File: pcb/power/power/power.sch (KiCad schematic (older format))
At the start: 14 parts, among them J1001 Conn_01x03_Female, J1002 Conn_01x04_Female, J1003 Conn_01x03_Female

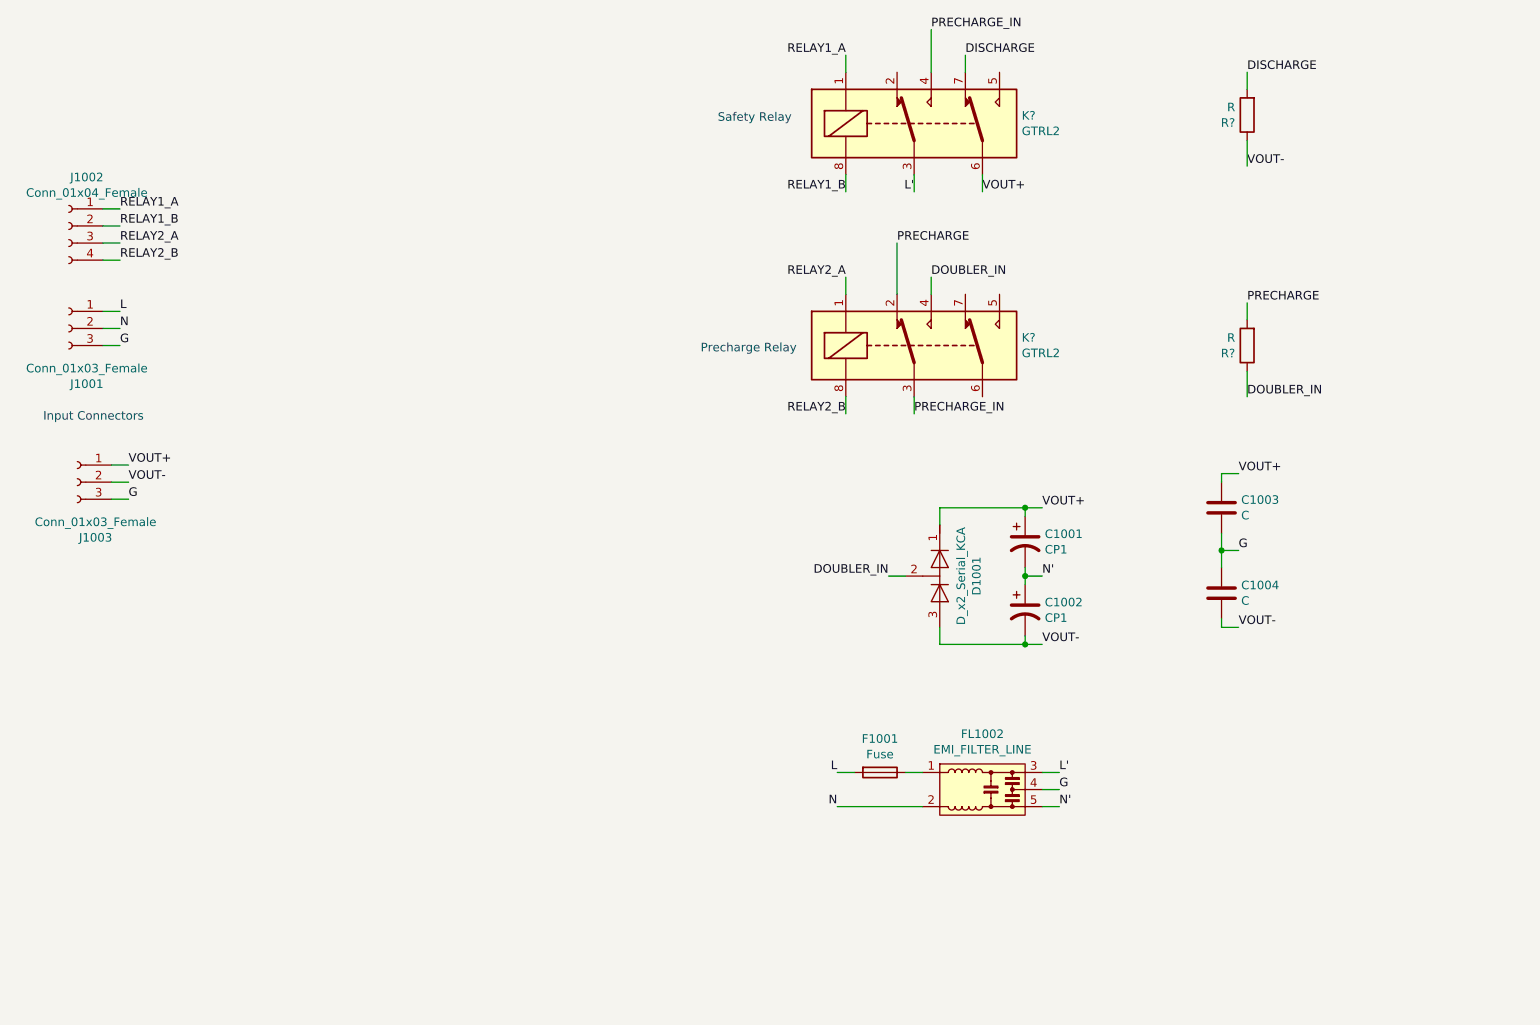
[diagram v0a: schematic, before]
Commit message: finished power and MMC PCBs and created gerbers
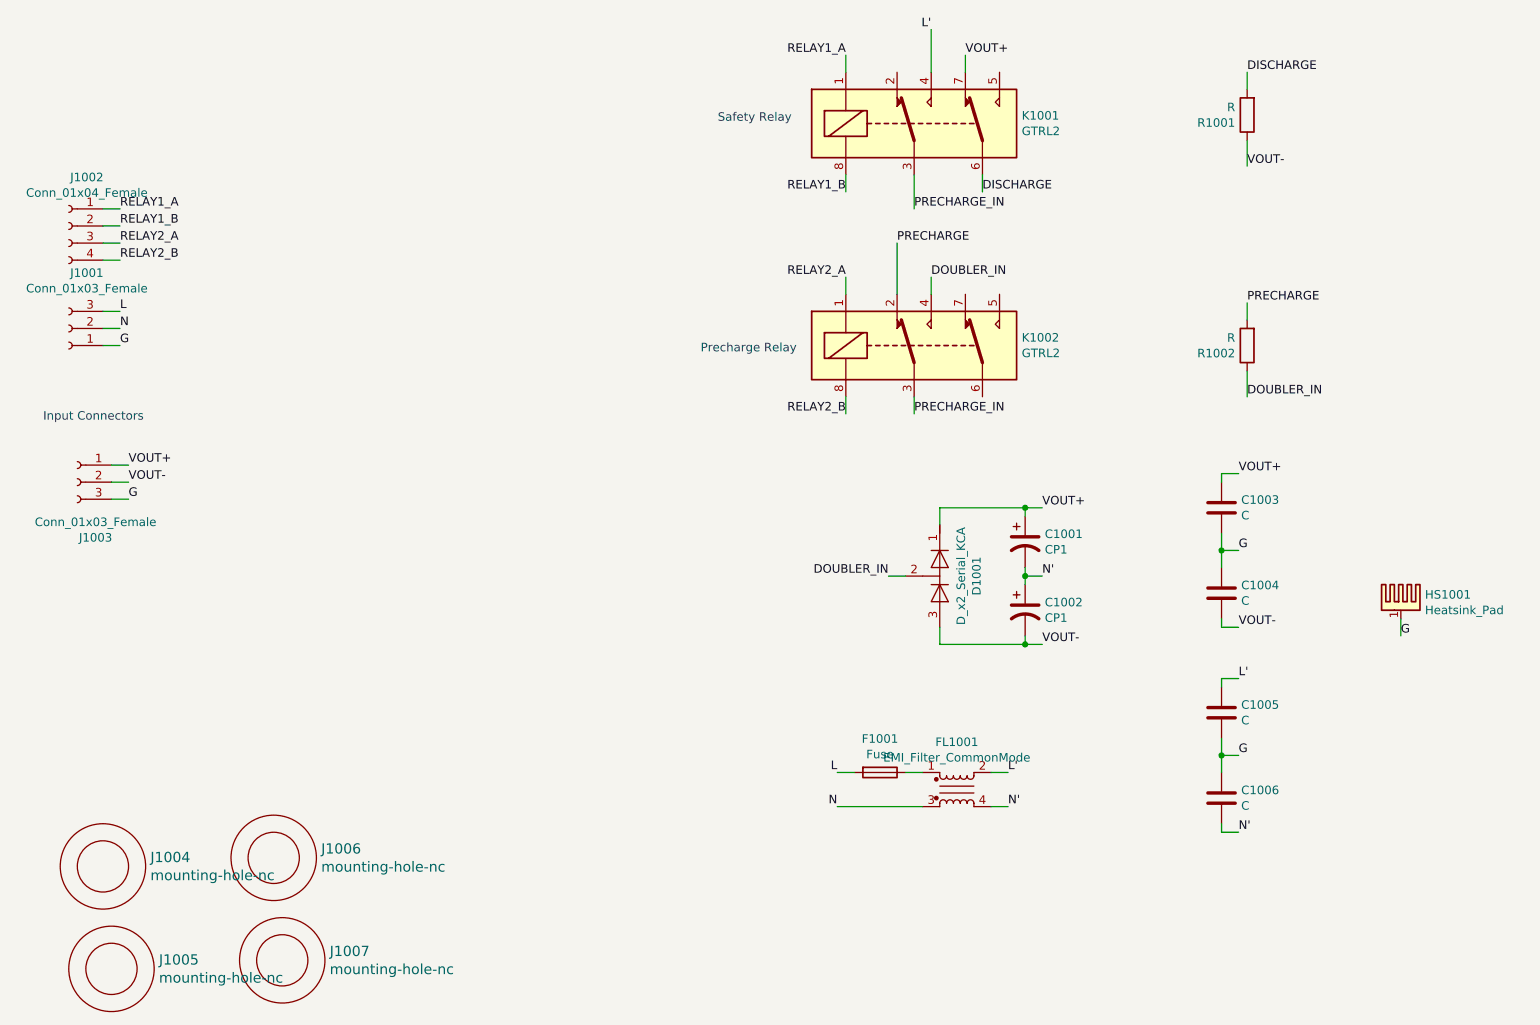
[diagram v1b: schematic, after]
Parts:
- removed FL1002: EMI_FILTER_LINE, symbol wbraun_ic_lib:EMI_FILTER_LINE
- added C1005, C1006: C, Capacitor_THT:C_Rect_L18.0mm_W8.0mm_P15.00mm_FKS3_FKP3, symbol Device:C
- added FL1001: EMI_Filter_CommonMode, wbraun_smd:744824622, symbol Device:EMI_Filter_CommonMode
- added HS1001: Heatsink_Pad, wbraun_smd:RA-T2X, symbol Mechanical:Heatsink_Pad
- added J1004, J1005, J1006, J1007: mounting-hole-nc, wbraun_smd:M3-mounting-hole-insulated, symbol wbraun_ic_lib:mounting-hole-nc
- C1001, C1002: footprint (none) -> Capacitor_THT:CP_Radial_D25.0mm_P10.00mm_SnapIn
- C1003, C1004: footprint (none) -> Capacitor_THT:C_Rect_L18.0mm_W8.0mm_P15.00mm_FKS3_FKP3
- D1001: footprint (none) -> Package_TO_SOT_THT:TO-247-3_Vertical
- J1001, J1003: footprint (none) -> wbraun_smd:Terminal-block-plug_3x1_5mm-pitch
- J1002: footprint (none) -> wbraun_smd:Terminal-block-plug_4x1_3.5mm-pitch
- K1001, K1002: renamed from K?; footprint (none) -> wbraun_smd:G2RL-2
- R1001, R1002: renamed from R?; footprint (none) -> wbraun_smd:RESISTOR_CW010
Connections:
- net DISCHARGE: now also K1001.6; no longer K1001.7
- net G: now also J1001.1 (Pin_1), C1005.2, C1006.1, HS1001.1; no longer J1001.3 (Pin_3)
- net L: now also J1001.3 (Pin_3); no longer J1001.1 (Pin_1)
- net L': now also K1001.4, C1005.1, FL1001.2; no longer K1001.3
- net N: now also FL1001.3
- net N': now also C1006.2, FL1001.4
- net PRECHARGE_IN: now also K1001.3; no longer K1001.4
- net VOUT+: now also K1001.7; no longer K1001.6
- net at F1001.1: now also FL1001.1
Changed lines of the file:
@@
 EESchema Schematic File Version 4
+LIBS:power-cache
 EELAYER 26 0
 EELAYER END
@@
 F 0 "J1002" H 1944 2285 50  0000 C CNN
 F 1 "Conn_01x04_Female" H 1944 2194 50  0000 C CNN
-F 2 "" H 2050 2000 50  0001 C CNN
+F 2 "wbraun_smd:Terminal-block-plug_4x1_3.5mm-pitch" H 2050 2000 50  0001 C CNN
 F 3 "~" H 2050 2000 50  0001 C CNN
 	1    2050 2000
@@
 F 0 "C1001" H 7765 3896 50  0000 L CNN
 F 1 "CP1" H 7765 3805 50  0000 L CNN
-F 2 "" H 7650 3850 50  0001 C CNN
+F 2 "Capacitor_THT:CP_Radial_D25.0mm_P10.00mm_SnapIn" H 7650 3850 50  0001 C CNN
 F 3 "~" H 7650 3850 50  0001 C CNN
 	1    7650 3850
@@
 F 0 "D1001" H 7150 4266 50  0000 C CNN
 F 1 "D_x2_Serial_KCA" H 7150 4175 50  0000 C CNN
-F 2 "" H 7150 4050 50  0001 C CNN
+F 2 "Package_TO_SOT_THT:TO-247-3_Vertical" H 7150 4050 50  0001 C CNN
 F 3 "~" H 7150 4050 50  0001 C CNN
 	1    7150 4050
@@
 F 0 "C1003" H 8915 3696 50  0000 L CNN
 F 1 "C" H 8915 3605 50  0000 L CNN
-F 2 "" H 8838 3500 50  0001 C CNN
+F 2 "Capacitor_THT:C_Rect_L18.0mm_W8.0mm_P15.00mm_FKS3_FKP3" H 8838 3500 50  0001 C CNN
 F 3 "~" H 8800 3650 50  0001 C CNN
 	1    8800 3650
@@
 F 0 "C1004" H 8915 4196 50  0000 L CNN
 F 1 "C" H 8915 4105 50  0000 L CNN
-F 2 "" H 8838 4000 50  0001 C CNN
+F 2 "Capacitor_THT:C_Rect_L18.0mm_W8.0mm_P15.00mm_FKS3_FKP3" H 8838 4000 50  0001 C CNN
 F 3 "~" H 8800 4150 50  0001 C CNN
 	1    8800 4150
@@
 F 0 "J1001" H 1944 2275 50  0000 C CNN
 F 1 "Conn_01x03_Female" H 1944 2366 50  0000 C CNN
-F 2 "" H 2050 2600 50  0001 C CNN
+F 2 "wbraun_smd:Terminal-block-plug_3x1_5mm-pitch" H 2050 2600 50  0001 C CNN
 F 3 "~" H 2050 2600 50  0001 C CNN
 	1    2050 2600
-	-1   0    0    -1
-$EndComp
-$Comp
-L wbraun_ic_lib:EMI_FILTER_LINE FL1002
-U 1 1 5C48EEA0
-P 7400 5300
-F 0 "FL1002" H 7400 5625 50  0000 C CNN
-F 1 "EMI_FILTER_LINE" H 7400 5534 50  0000 C CNN
-F 2 "" H 7400 5300 50  0001 C CNN
-F 3 "" H 7400 5300 50  0001 C CNN
-	1    7400 5300
-	1    0    0    -1
+	-1   0    0    1
 $EndComp
 $Comp
@@
 	6650 5200 6550 5200
 Wire Wire Line
-	7750 5200 7850 5200
-Wire Wire Line
-	7750 5300 7850 5300
-Wire Wire Line
-	7750 5400 7850 5400
+	7450 5200 7550 5200
+Wire Wire Line
+	7450 5400 7550 5400
 Text Label 6550 5200 2    50   ~ 0
 L
 Text Label 6550 5400 2    50   ~ 0
 N
-Text Label 7850 5200 0    50   ~ 0
+Text Label 7550 5200 0    50   ~ 0
 L'
-Text Label 7850 5400 0    50   ~ 0
+Text Label 7550 5400 0    50   ~ 0
 N'
-Text Label 7850 5300 0    50   ~ 0
-G
-$Comp
-L wbraun_ic_lib:GTRL2 K?
+$Comp
+L wbraun_ic_lib:GTRL2 K1001
 U 1 1 5C496070
 P 7000 1400
-F 0 "K?" H 7630 1446 50  0000 L CNN
+F 0 "K1001" H 7630 1446 50  0000 L CNN
 F 1 "GTRL2" H 7630 1355 50  0000 L CNN
-F 2 "" H 6950 1400 50  0001 C CNN
+F 2 "wbraun_smd:G2RL-2" H 6950 1400 50  0001 C CNN
 F 3 "" H 6950 1400 50  0001 C CNN
 	1    7000 1400
@@
 $EndComp
 $Comp
-L wbraun_ic_lib:GTRL2 K?
+L wbraun_ic_lib:GTRL2 K1002
 U 1 1 5C4963A0
 P 7000 2700
-F 0 "K?" H 7630 2746 50  0000 L CNN
+F 0 "K1002" H 7630 2746 50  0000 L CNN
 F 1 "GTRL2" H 7630 2655 50  0000 L CNN
-F 2 "" H 6950 2700 50  0001 C CNN
+F 2 "wbraun_smd:G2RL-2" H 6950 2700 50  0001 C CNN
 F 3 "" H 6950 2700 50  0001 C CNN
 	1    7000 2700
@@
 Text Label 6600 1800 2    50   ~ 0
 RELAY1_B
-Wire Wire Line
-	7000 1700 7000 1800
-Text Label 7000 1800 2    50   ~ 0
+Text Label 7100 850  2    50   ~ 0
 L'
 Wire Wire Line
@@
 Wire Wire Line
 	7300 1100 7300 1000
+Text Label 7300 1000 0    50   ~ 0
+VOUT+
 Text Label 7400 1800 0    50   ~ 0
-VOUT+
-Text Label 7300 1000 0    50   ~ 0
 DISCHARGE
 Text Label 7000 3100 0    50   ~ 0
@@
 Wire Wire Line
 	7100 2400 7100 2300
-Text Label 7100 850  0    50   ~ 0
+Text Label 7000 1900 0    50   ~ 0
 PRECHARGE_IN
 Wire Wire Line
@@
 DOUBLER_IN
 $Comp
-L Device:R R?
+L Device:R R1001
 U 1 1 5C498F2D
 P 8950 1350
-F 0 "R?" H 9020 1396 50  0000 L CNN
+F 0 "R1001" H 9020 1396 50  0000 L CNN
 F 1 "R" H 9020 1305 50  0000 L CNN
-F 2 "" V 8880 1350 50  0001 C CNN
+F 2 "wbraun_smd:RESISTOR_CW010" V 8880 1350 50  0001 C CNN
 F 3 "~" H 8950 1350 50  0001 C CNN
 	1    8950 1350
@@
 VOUT-
 $Comp
-L Device:R R?
+L Device:R R1002
 U 1 1 5C499891
 P 8950 2700
-F 0 "R?" H 9020 2746 50  0000 L CNN
+F 0 "R1002" H 9020 2746 50  0000 L CNN
 F 1 "R" H 9020 2655 50  0000 L CNN
-F 2 "" V 8880 2700 50  0001 C CNN
+F 2 "wbraun_smd:RESISTOR_CW010" V 8880 2700 50  0001 C CNN
 F 3 "~" H 8950 2700 50  0001 C CNN
 	1    8950 2700
@@
 F 0 "C1002" H 7765 4296 50  0000 L CNN
 F 1 "CP1" H 7765 4205 50  0000 L CNN
-F 2 "" H 7650 4250 50  0001 C CNN
+F 2 "Capacitor_THT:CP_Radial_D25.0mm_P10.00mm_SnapIn" H 7650 4250 50  0001 C CNN
 F 3 "~" H 7650 4250 50  0001 C CNN
 	1    7650 4250
@@
 N'
 Wire Wire Line
-	8800 3800 8800 3900
-Wire Wire Line
 	8800 3900 8900 3900
-Connection ~ 8800 3900
-Wire Wire Line
-	8800 3900 8800 4000
 Wire Wire Line
 	8800 3500 8800 3450
@@
 F 0 "J1003" H 1993 3175 50  0000 C CNN
 F 1 "Conn_01x03_Female" H 1993 3266 50  0000 C CNN
-F 2 "" H 2100 3500 50  0001 C CNN
+F 2 "wbraun_smd:Terminal-block-plug_3x1_5mm-pitch" H 2100 3500 50  0001 C CNN
 F 3 "~" H 2100 3500 50  0001 C CNN
 	1    2100 3500
@@
 Text Label 2400 3600 0    50   ~ 0
 G
+$Comp
+L Mechanical:Heatsink_Pad HS1001
+U 1 1 5C4B8180
+P 9850 4200
+F 0 "HS1001" H 9991 4241 50  0000 L CNN
+F 1 "Heatsink_Pad" H 9991 4150 50  0000 L CNN
+F 2 "wbraun_smd:RA-T2X" H 9862 4150 50  0001 C CNN
+F 3 "~" H 9862 4150 50  0001 C CNN
+	1    9850 4200
+	1    0    0    -1
+$EndComp
+$Comp
+L Device:EMI_Filter_CommonMode FL1001
+U 1 1 5C4AA415
+P 7250 5300
+F 0 "FL1001" H 7250 5578 50  0000 C CNN
+F 1 "EMI_Filter_CommonMode" H 7250 5487 50  0000 C CNN
+F 2 "wbraun_smd:744824622" V 7250 5340 50  0001 C CNN
+F 3 "~" V 7250 5340 50  0000 C CNN
+	1    7250 5300
+	1    0    0    -1
+$EndComp
+Wire Wire Line
+	8800 3800 8800 3900
+Wire Wire Line
+	8800 3900 8800 4000
+Connection ~ 8800 3900
+Text Label 9850 4400 0    50   ~ 0
+G
+Wire Wire Line
+	9850 4300 9850 4400
+$Comp
+L wbraun_ic_lib:mounting-hole-nc J1004
+U 1 1 5C4AE651
+P 2250 5750
+F 0 "J1004" H 2528 5803 60  0000 L CNN
+F 1 "mounting-hole-nc" H 2528 5697 60  0000 L CNN
+F 2 "wbraun_smd:M3-mounting-hole-insulated" H 2250 5750 60  0001 C CNN
+F 3 "" H 2250 5750 60  0001 C CNN
+	1    2250 5750
+	1    0    0    -1
+$EndComp
+$Comp
+L wbraun_ic_lib:mounting-hole-nc J1006
+U 1 1 5C4AE7C3
+P 3250 5700
+F 0 "J1006" H 3528 5753 60  0000 L CNN
+F 1 "mounting-hole-nc" H 3528 5647 60  0000 L CNN
+F 2 "wbraun_smd:M3-mounting-hole-insulated" H 3250 5700 60  0001 C CNN
+F 3 "" H 3250 5700 60  0001 C CNN
+	1    3250 5700
+	1    0    0    -1
+$EndComp
+$Comp
+L wbraun_ic_lib:mounting-hole-nc J1007
+U 1 1 5C4AE82D
+P 3300 6300
+F 0 "J1007" H 3578 6353 60  0000 L CNN
+F 1 "mounting-hole-nc" H 3578 6247 60  0000 L CNN
+F 2 "wbraun_smd:M3-mounting-hole-insulated" H 3300 6300 60  0001 C CNN
+F 3 "" H 3300 6300 60  0001 C CNN
+	1    3300 6300
+	1    0    0    -1
+$EndComp
+$Comp
+L wbraun_ic_lib:mounting-hole-nc J1005
+U 1 1 5C4AE887
+P 2300 6350
+F 0 "J1005" H 2578 6403 60  0000 L CNN
+F 1 "mounting-hole-nc" H 2578 6297 60  0000 L CNN
+F 2 "wbraun_smd:M3-mounting-hole-insulated" H 2300 6350 60  0001 C CNN
+F 3 "" H 2300 6350 60  0001 C CNN
+	1    2300 6350
+	1    0    0    -1
+$EndComp
+$Comp
+L Device:C C1005
+U 1 1 5C4B11B7
+P 8800 4850
+F 0 "C1005" H 8915 4896 50  0000 L CNN
+F 1 "C" H 8915 4805 50  0000 L CNN
+F 2 "Capacitor_THT:C_Rect_L18.0mm_W8.0mm_P15.00mm_FKS3_FKP3" H 8838 4700 50  0001 C CNN
+F 3 "~" H 8800 4850 50  0001 C CNN
+	1    8800 4850
+	1    0    0    -1
+$EndComp
+$Comp
+L Device:C C1006
+U 1 1 5C4B11BE
+P 8800 5350
+F 0 "C1006" H 8915 5396 50  0000 L CNN
+F 1 "C" H 8915 5305 50  0000 L CNN
+F 2 "Capacitor_THT:C_Rect_L18.0mm_W8.0mm_P15.00mm_FKS3_FKP3" H 8838 5200 50  0001 C CNN
+F 3 "~" H 8800 5350 50  0001 C CNN
+	1    8800 5350
+	1    0    0    -1
+$EndComp
+Wire Wire Line
+	8800 5100 8900 5100
+Wire Wire Line
+	8800 4700 8800 4650
+Wire Wire Line
+	8800 4650 8900 4650
+Wire Wire Line
+	8800 5500 8800 5550
+Wire Wire Line
+	8800 5550 8900 5550
+Text Label 8900 5100 0    50   ~ 0
+G
+Wire Wire Line
+	8800 5000 8800 5100
+Wire Wire Line
+	8800 5100 8800 5200
+Connection ~ 8800 5100
+Text Label 8900 4650 0    50   ~ 0
+L'
+Text Label 8900 5550 0    50   ~ 0
+N'
+Wire Wire Line
+	7000 1700 7000 1900
 $EndSCHEMATC
